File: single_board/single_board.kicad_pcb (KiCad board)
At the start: 4 copper layers, 118.6 x 108.9 mm, 121 parts, among them J1 SWD, J11 SPI Debug, J17 BOOTSEL, J2 USB_C_Receptacle_USB2.0_16P, J3 RST, J30 JST_GH_H, J31 JST_GH_H, J32 PB_Vertical, J33 JST_GH_H, J34 PB_Vertical, J35 JST_GH_H, J36 JST_GH_H, J37 JST_GH_H, J38 PB_Vertical, J39 PB_Vertical, J4 Conn_01x02, J40 PB_Vertical, J41 PB_Vertical, J42 PB_Vertical, J43 PB_Vertical, J44 PB_Vertical, J45 PB_Vertical, J46 PB_Vertical, J47 PB_Vertical, J48 PB_Vertical, J49 PB_Vertical, J5 Conn_01x02, J50 PB_Vertical, J6 Conn_01x02, J7 Conn_01x02, Q1 AO3401A, Q2 AO3401A, Q3 AO3401A, Q4 AO3401A, Q5 2N7002, SW1 Button, U1 AP2112K-3.3, U3 USBLC6-2SC6, U4 LSM6DSV, U5 STM32G474VBTx, Y1 FC-135

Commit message: PCB Layout
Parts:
- removed R32: 120, Resistor_SMD:R_0402_1005Metric
- moved C28 147.8 mm to (40.8, 118.8)
- moved R19 147.8 mm to (38.6, 118.8)
- moved SW1 147.8 mm to (39.7, 123.9)
- moved J3 141.1 mm to (43.8, 120.8)
- moved J50 107.9 mm to (90.0, 145.8)
- moved Q3 107.3 mm to (94.9, 122.0)
- moved R23 104.7 mm to (93.5, 119.2), turned to 90 degrees
- moved J5 100.5 mm to (67.8, 112.1)
- moved C37 98.6 mm to (88.7, 159.7), turned to 180 degrees
- moved C38 97.7 mm to (88.7, 160.7), turned to 180 degrees
- moved J1 96.9 mm to (88.6, 122.2), turned to 180 degrees
- moved J44 96.0 mm to (27.6, 131.3)
- moved J40 96.0 mm to (27.5, 148.4)
- moved J39 95.9 mm to (27.6, 140.1)
- moved C36 95.8 mm to (24.9, 134.3)
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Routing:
- net /ENC3_B: track 6.06 -> 40.4 mm
- net /ENC3_A: track 5.11 -> 38.9 mm
- net /RST: track 9.65 -> 42.3 mm
- net /FSR_ADC: track 5.26 -> 33.3 mm
- net /ENC6_B: track 5.01 -> 31.6 mm
- net /ENC2_A: track 6.90 -> 33.3 mm
- net /ENC6_A: track 5.57 -> 31.9 mm
- net /SWCLK: track 3.33 -> 29.3 mm
- net /ENC2_B: track 7.10 -> 32.9 mm
- net /SWDIO: track 2.99 -> 27.9 mm
- net /DIR2: track 3.35 -> 26.5 mm
- net /ENC1_A: track 8.30 -> 31.2 mm
- net /ENC1_B: track 8.20 -> 30.9 mm
- net /UART4_RX: track 4.04 -> 26.5 mm
- net /PWM6: track 4.10 -> 26.4 mm
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- added copper zone on In2.Cu, net /v3v3IN_debug
- removed copper zone on In2.Cu, net 5V
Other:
- board size 118.6 x 108.9 mm -> 111.9 x 102.9 mm
- board text removed: "GND"
- board text removed: "RX"
- board text removed: "TX"
- board text removed: "UART"

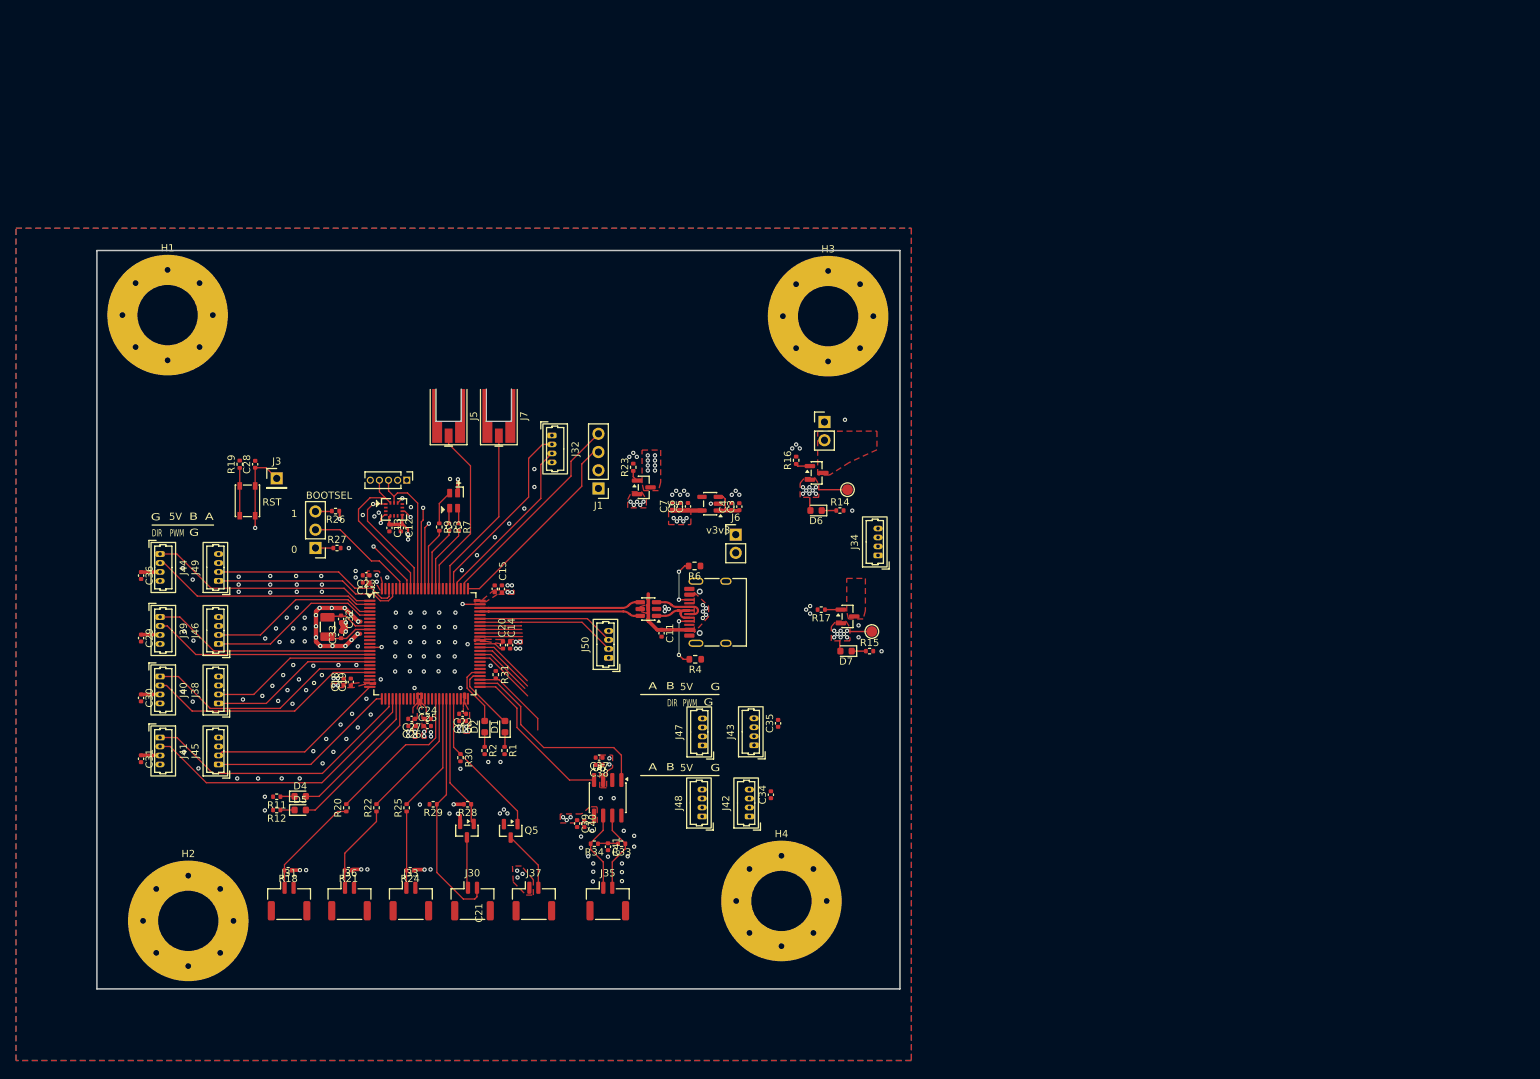
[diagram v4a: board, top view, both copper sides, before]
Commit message: Controls Board Version 0
Rough layout of Elec Controls Board. SIlkscreen in progress. New schematic changes have not been incorporated fully yet. SIzed 100 x 95 mm
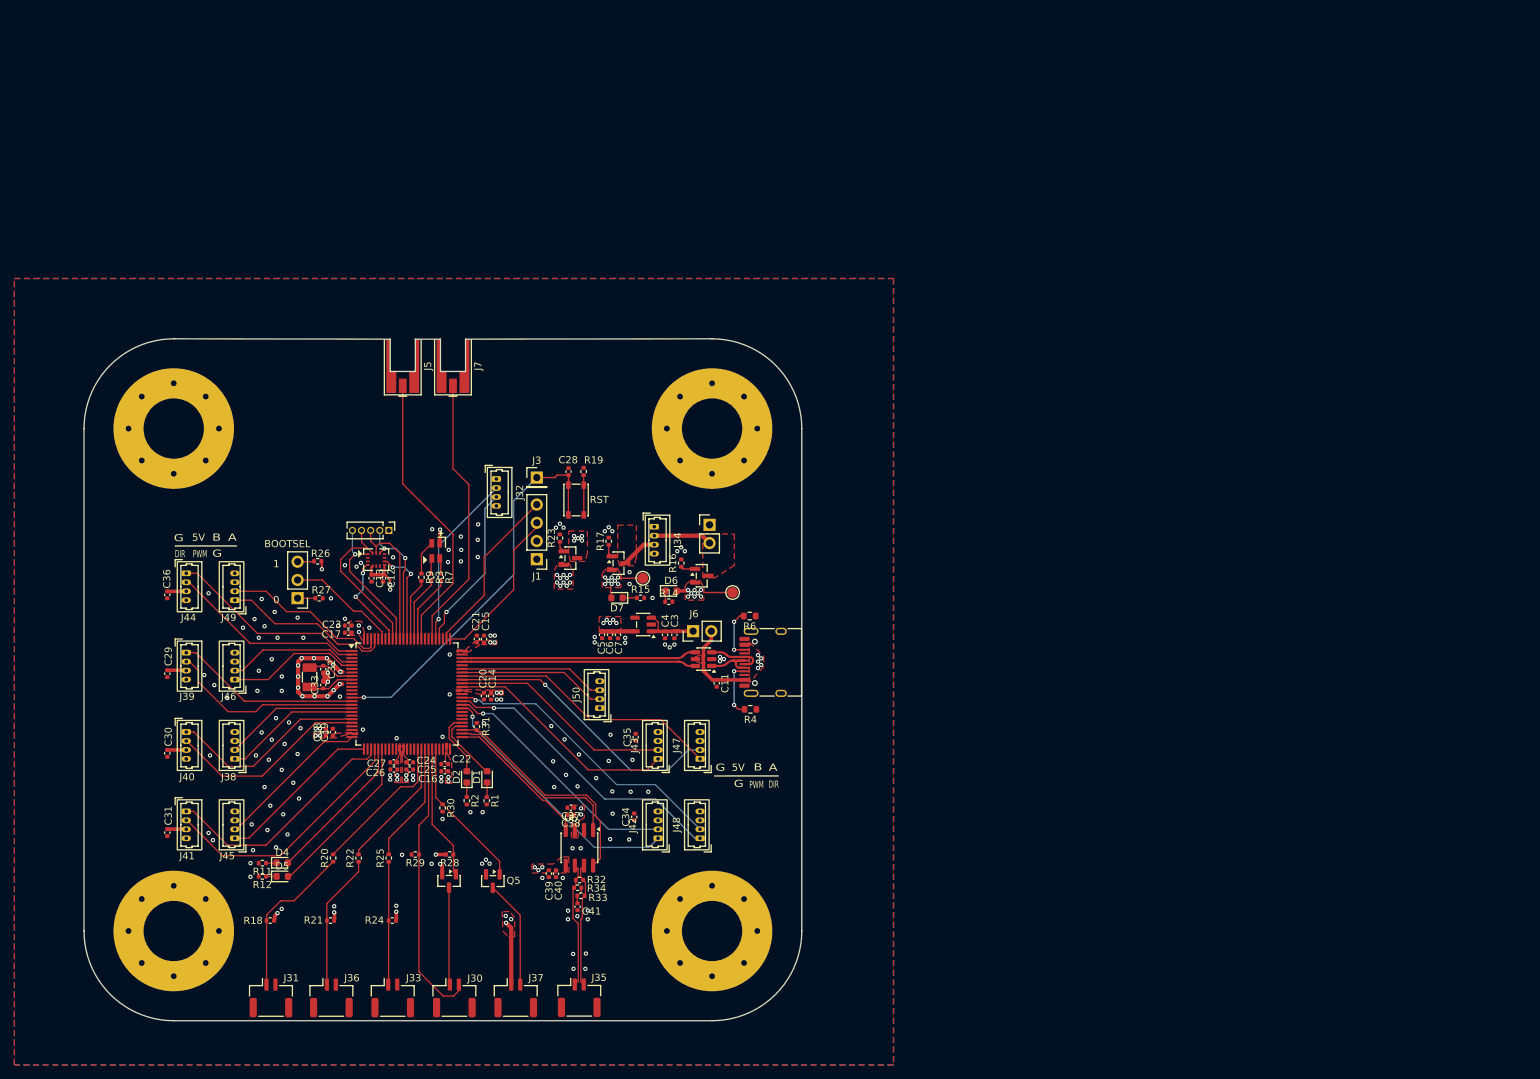
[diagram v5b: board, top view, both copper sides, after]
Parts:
- added R32: 120, Resistor_SMD:R_0402_1005Metric, F.Cu at (86.0, 176.8)
- moved R19 47.9 mm to (86.6, 119.8)
- moved SW1 45.8 mm to (85.5, 123.8), turned to -90 degrees
- moved C28 43.7 mm to (84.5, 119.9)
- moved J3 36.2 mm to (80.0, 120.7)
- moved D7 32.8 mm to (91.2, 137.4)
- moved R15 32.8 mm to (94.5, 137.4)
- moved Q2 32.8 mm to (91.4, 132.6)
- moved TP2 32.8 mm to (94.8, 134.7)
- moved J34 31.4 mm to (96.4, 127.5), turned to -90 degrees
- moved R17 31.1 mm to (90.1, 129.6), turned to 90 degrees
- moved R14 27.0 mm to (98.4, 138.0)
- moved D6 23.1 mm to (98.8, 136.5), turned to 0 degrees
- moved H3 22.5 mm to (104.5, 113.9)
- moved C5 21.5 mm to (89.1, 142.6), turned to -90 degrees
- moved J4 21.5 mm to (104.1, 127.3)
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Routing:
- net /PWM4: track 5.84 -> 39.5 mm, vias 0 -> 1
- net /DIR5: track 8.65 -> 41.1 mm, vias 0 -> 1
- net /PWM5: track 8.53 -> 40.8 mm, vias 0 -> 1
- net /DIR4: track 5.75 -> 37.9 mm
- net /ENC4_A: track 8.84 -> 36.9 mm, vias 0 -> 1
- net /ENC5_A: track 5.94 -> 32.7 mm
- net /ENC4_B: track 8.21 -> 34.5 mm, vias 0 -> 1
- net /ENC5_B: track 5.89 -> 31.1 mm
- net /CAN_STB: track 11.9 -> 32.1 mm
- net /UART5_RX: track 24.4 -> 40.0 mm
- net /UART5_TX: track 24.1 -> 38.3 mm
- net /RST: track 42.3 -> 54.6 mm, vias 2 -> 1
- net /USB-DN: track 22.5 -> 32.7 mm
- net /USB-DP: track 22.5 -> 32.7 mm
- net v3v3: track 48.3 -> 57.2 mm, vias 47 -> 52
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- added copper zone on In2.Cu, net 5V
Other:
- board size 111.9 x 102.9 mm -> 100 x 95 mm
- board text removed: "v3v3"

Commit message: Controls Board
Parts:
- moved C11 0.06 mm to (105.0, 149.3)
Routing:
- net v3v3: track 57.2 -> 67.9 mm
- net 5V: track 30.4 -> 36.9 mm
- net /PWM5: track 40.8 -> 42.7 mm
- net /DIR5: track 41.1 -> 42.8 mm

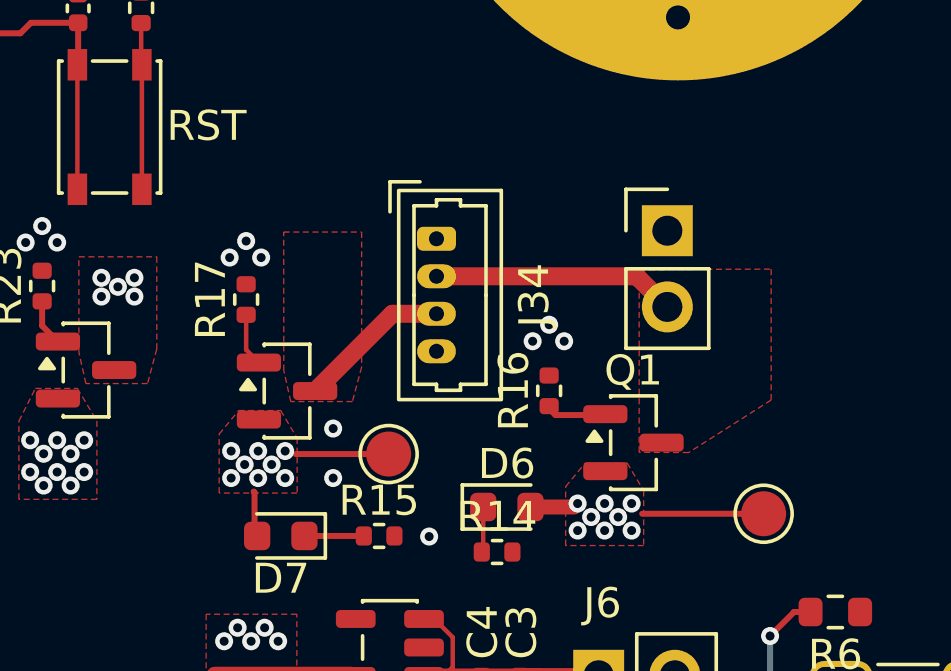
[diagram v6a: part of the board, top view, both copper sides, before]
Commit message: Updated schematic (power)
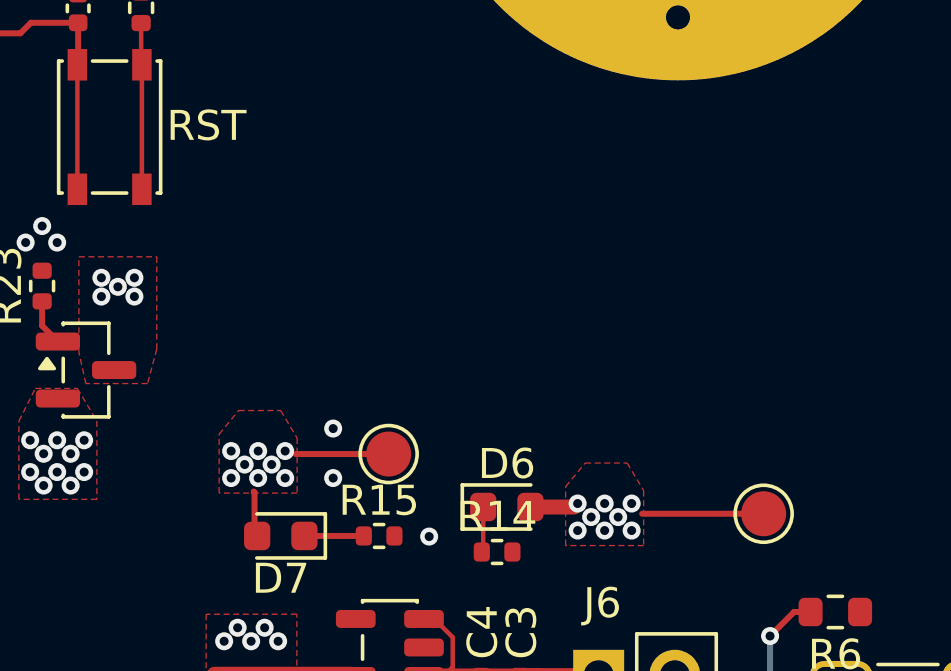
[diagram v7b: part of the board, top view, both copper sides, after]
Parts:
- removed J34: PB_Vertical, Connector_Molex:Molex_PicoBlade_53047-0410_1x04_P1.25mm_Vertical
- removed J4: Conn_01x02, Connector_PinHeader_2.54mm:PinHeader_1x02_P2.54mm_Vertical
- removed Q1, Q2: AO3401A, Package_TO_SOT_SMD:SOT-23
- removed R16, R17: 10k, Resistor_SMD:R_0402_1005Metric
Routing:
- net /5VIN: track 8.12 -> 0.00 mm
- net /v3v3IN: track 5.11 -> 0.00 mm
- net Net-(Q1-G): track 2.00 -> 0.00 mm
- net Net-(Q2-G): track 1.77 -> 0.00 mm
- net GND: vias 157 -> 151
- removed copper zone on F.Cu, net /5VIN
- removed copper zone on F.Cu, net /v3v3IN
